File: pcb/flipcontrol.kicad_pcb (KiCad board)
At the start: 4 copper layers, 133.3 x 61.6 mm, 96 parts, among them J1 PJ-202A, J2 DOT_BOARD_1, J3 DOT_BOARD_2, J4 LED_STRIP, J5 DOT_BOARD_3, J6 RJMG163118101NR, J7 FTDI, Q2 Si2347DS-T1-GE3, Q3 MMBT3904, Q4 Si2347DS-T1-GE3, Q5 MMBT3904, U1 TPS563300, U2 AMS1117-3.3, U3 ESP32-S3-WROOM-1, U4 NCS214, U5 W5500, Y1 Crystal_GND24

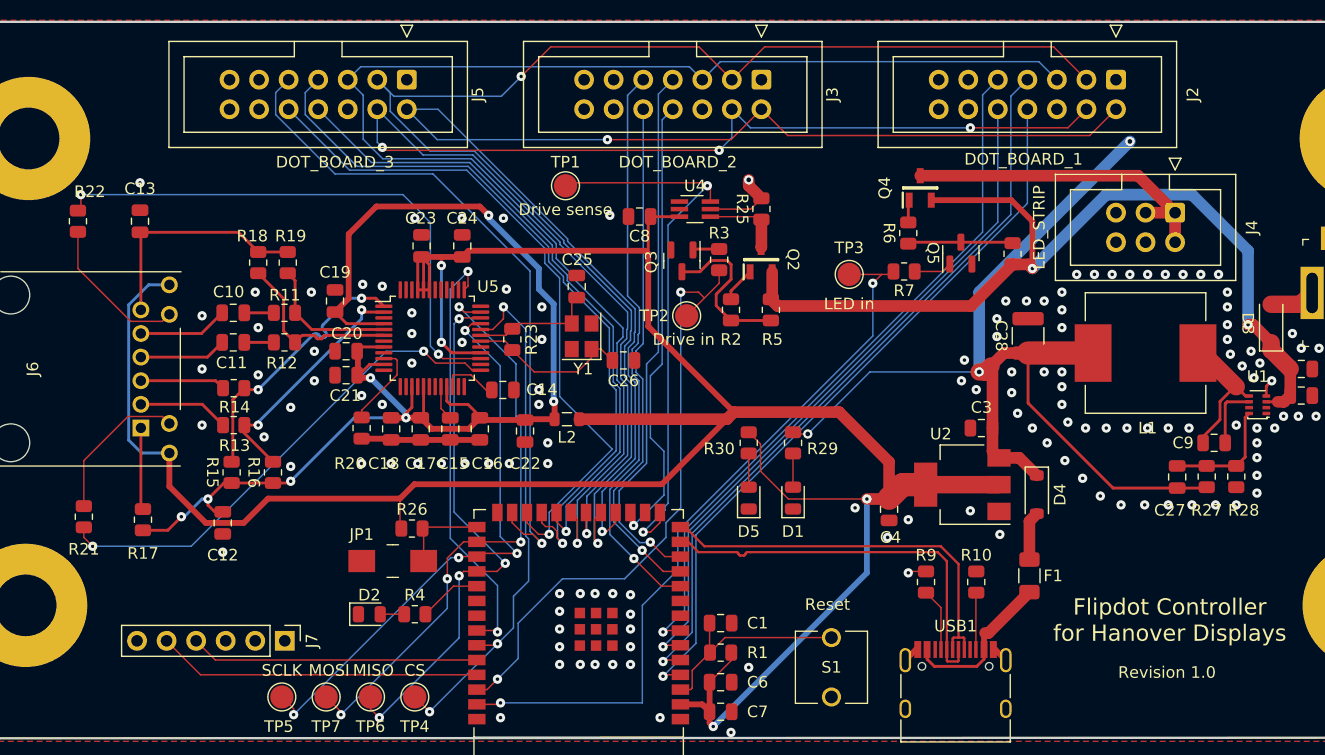
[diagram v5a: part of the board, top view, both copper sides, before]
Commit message: Make panel pin 14 constantly powered with 18V
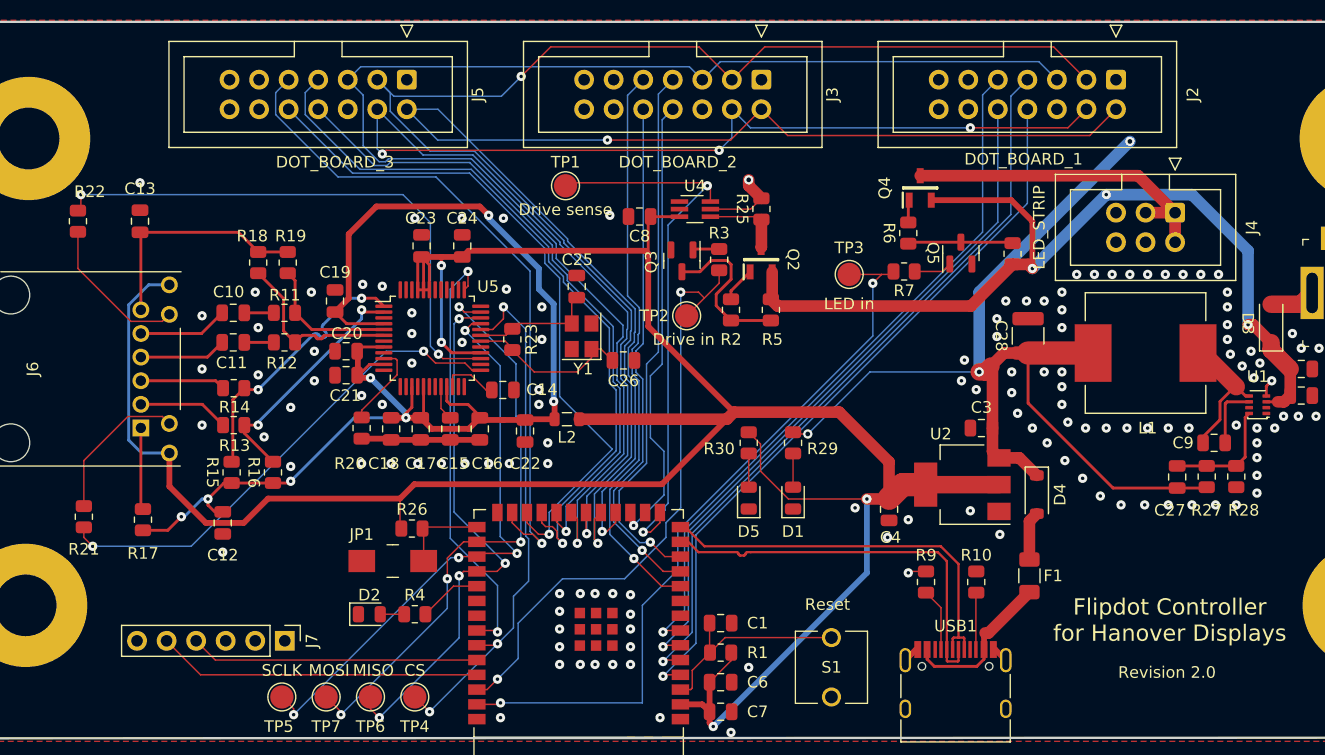
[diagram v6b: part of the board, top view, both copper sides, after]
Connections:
- J2 pad 14: COIL_DRIVE_OUT -> +18V
- J3 pad 14: COIL_DRIVE_OUT -> +18V
- J5 pad 14: COIL_DRIVE_OUT -> +18V
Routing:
- net +18V: track 79.9 -> 162.1 mm, vias 2 -> 3
- net COIL_DRIVE_OUT: track 87.9 -> 82.7 mm
- net ENABLE_3: track 120.0 -> 120.6 mm
- net ENABLE_4: track 122.2 -> 122.8 mm
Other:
- board text added: "Revision 2.0"
- board text removed: "Revision 1.0"

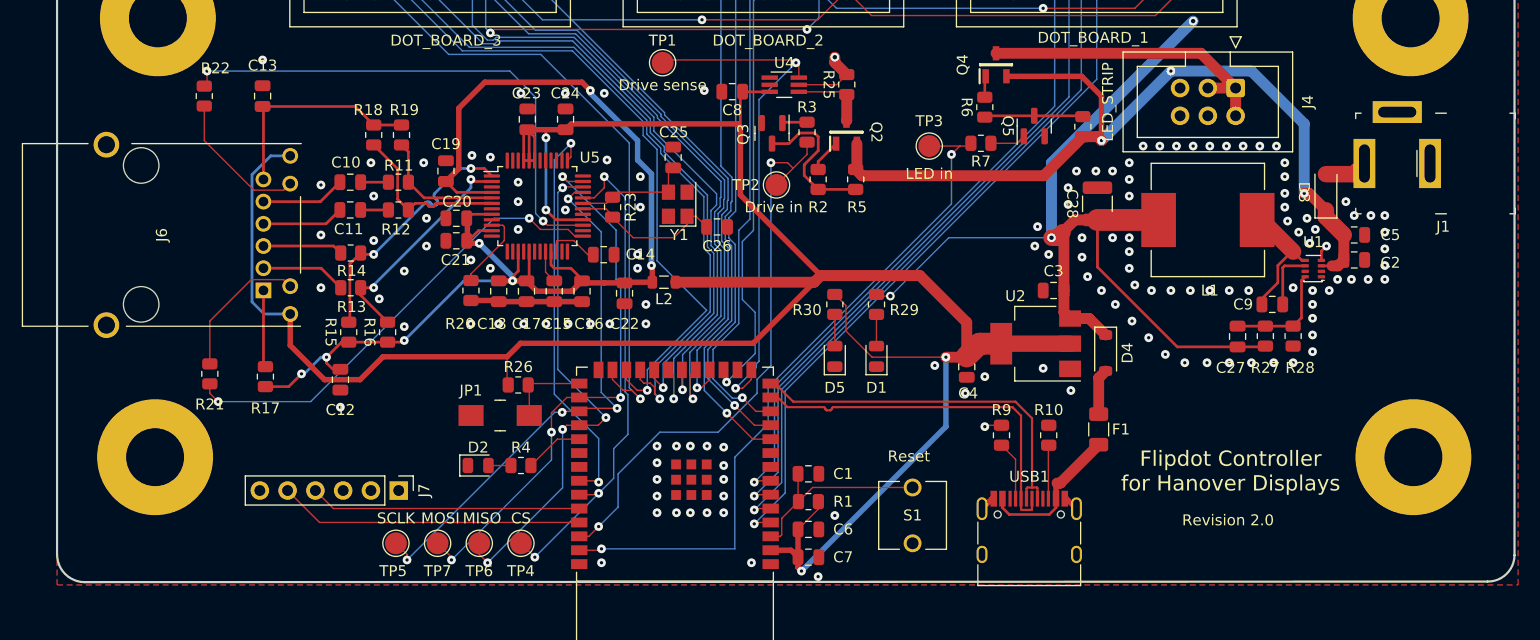
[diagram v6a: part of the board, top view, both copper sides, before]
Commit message: Update PCB to use more JLCPCB parts for power supply
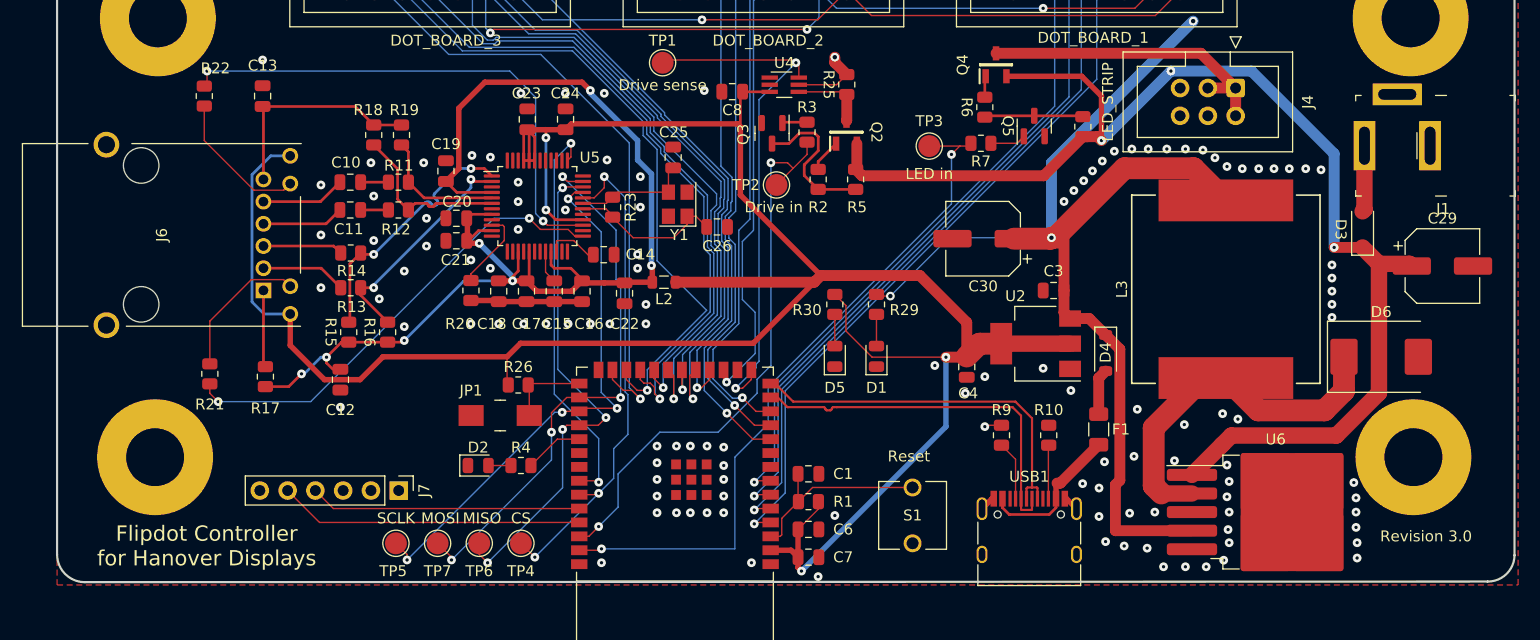
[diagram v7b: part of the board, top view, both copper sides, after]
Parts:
- removed C2: 10uF 2.8mΩ 35V, Capacitor_SMD:C_0805_2012Metric
- removed C27: 47 pF, Capacitor_SMD:C_0805_2012Metric
- removed C28: 47uF 3mΩ 16V, Capacitor_SMD:C_1210_3225Metric
- removed C5: 100nF 30mΩ 50V, Capacitor_SMD:C_0805_2012Metric
- removed C9: 100 nF 1mΩ 10V, Capacitor_SMD:C_0805_2012Metric
- removed L1: IHLP4040DZER6R8M01, Inductor_SMD:L_Vishay_IHLP-4040
- removed R27: 52.3k, Resistor_SMD:R_0805_2012Metric
- removed R28: 10k, Resistor_SMD:R_0805_2012Metric
- removed U1: TPS563300, Package_TO_SOT_SMD:SOT-583-8
- added C29: 100uF, Capacitor_SMD:CP_Elec_6.3x5.4, F.Cu at (212.3, 98.1)
- added C30: 330uF, Capacitor_SMD:CP_Elec_6.3x5.4, F.Cu at (170.3, 95.6)
- added D6: 700mV 5A, Diode_SMD:D_SMC, F.Cu at (206.7, 106.4)
- added L3: 47uH, Inductor_SMD:L_Vishay_IHLP-6767, F.Cu at (192.5, 100.2)
- added U6: LM2596S-5, Package_TO_SOT_SMD:TO-263-5_TabPin3, F.Cu at (197.1, 120.6)
- C22: value 10uF/16V -> 10uF
- C23: value 10uF/16v -> 10uF
- L2: value HH-1M1608-121JT -> ~
- R20: value 12.4k 1% -> 12.4k
- R29: value R_Small -> 145R
- R30: value R_Small -> 60R
- moved D3 4.78 mm to (205.0, 94.7)
- moved J1 1.62 mm to (208.2, 87.1)
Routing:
- net +18V: track 162.1 -> 197.9 mm
- net Net-(D6-K): track 0.00 -> 34.8 mm
- net +5V: track 185.3 -> 201.0 mm
- net Net-(U1-SW): track 12.0 -> 0.00 mm
- net Net-(U1-VFB): track 10.0 -> 0.00 mm
- net Net-(U1-VBST): track 5.49 -> 0.00 mm
- net Net-(D3-A): track 3.93 -> 6.07 mm
- net GND: track 16.2 -> 14.7 mm, vias 139 -> 121
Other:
- board text added: "Revision 3.0"
- board text removed: "Revision 2.0"

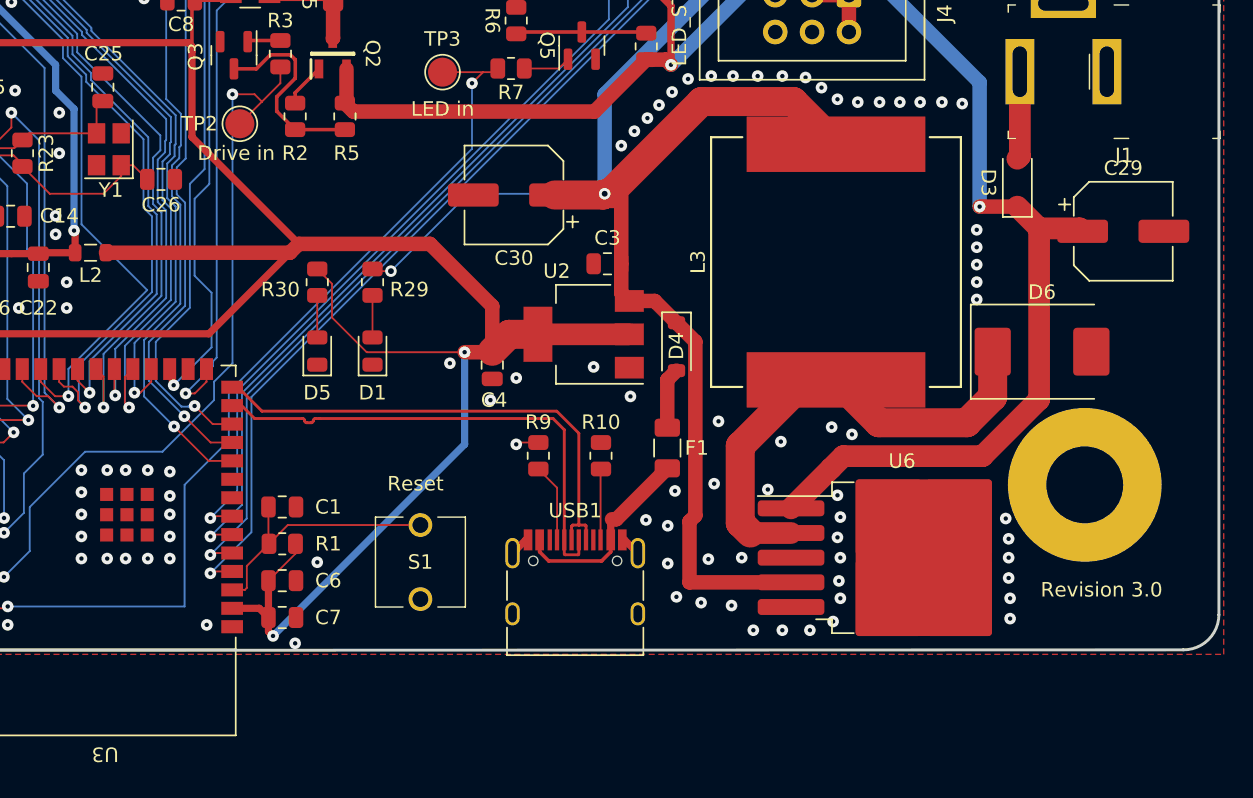
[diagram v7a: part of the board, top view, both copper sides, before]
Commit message: Rev4: Make more parts JLCPCB assembly service compatible
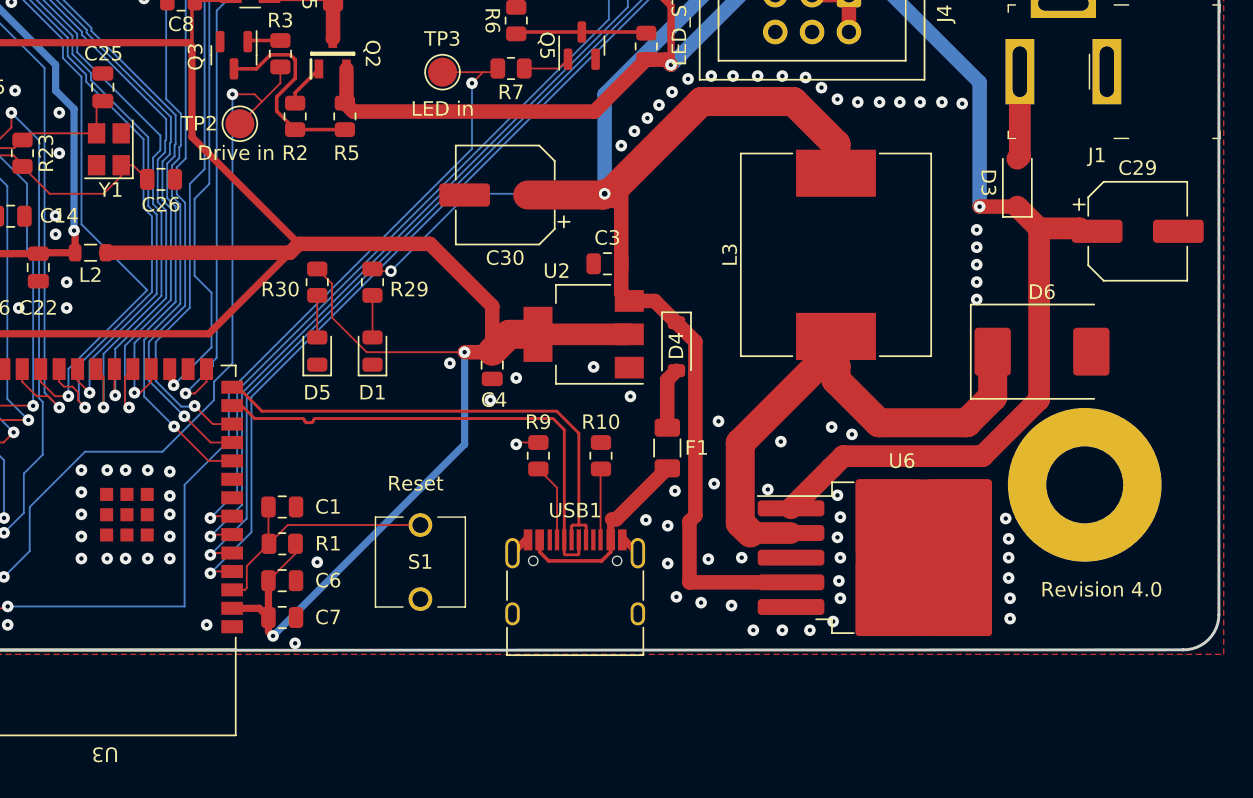
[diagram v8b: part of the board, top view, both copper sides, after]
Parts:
- L2: value ~ -> 120Ohms@100MHz
- L3: footprint Inductor_SMD:L_Vishay_IHLP-6767 -> Inductor_SMD:L_Sunlord_MWSA1206S-470
- moved C29 1.00 mm to (213.3, 98.1)
- moved C30 0.60 mm to (169.7, 95.6)
- moved L3 0.50 mm to (192.5, 99.7)
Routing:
- net +5V: track 201.0 -> 203.7 mm
- net +18V: track 197.9 -> 199.7 mm
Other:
- board text added: "Revision 4.0"
- board text removed: "Revision 3.0"
